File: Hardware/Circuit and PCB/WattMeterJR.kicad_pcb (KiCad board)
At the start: 4 copper layers, 66.6 x 82.1 mm, 51 parts, among them IC1 ATM90E32AS-AU-R, J1 502570-0893, J5 Input, J6 Debug, J7 PWR/GND, T1 CT1020, U2 ESP32-C6-WROOM-1-N8, Y1 16.384MHz

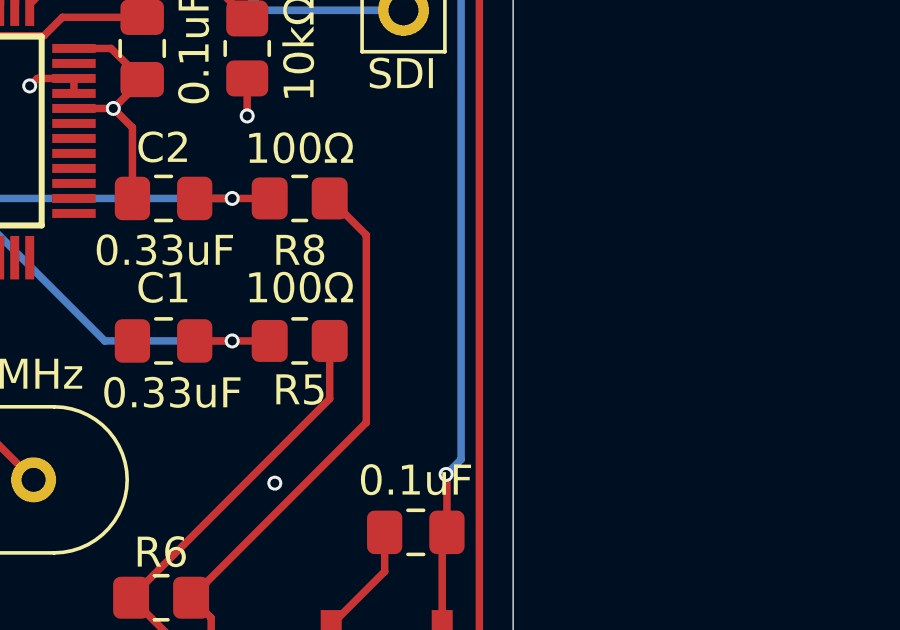
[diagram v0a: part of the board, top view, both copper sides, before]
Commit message: Add pullup for GPIO9
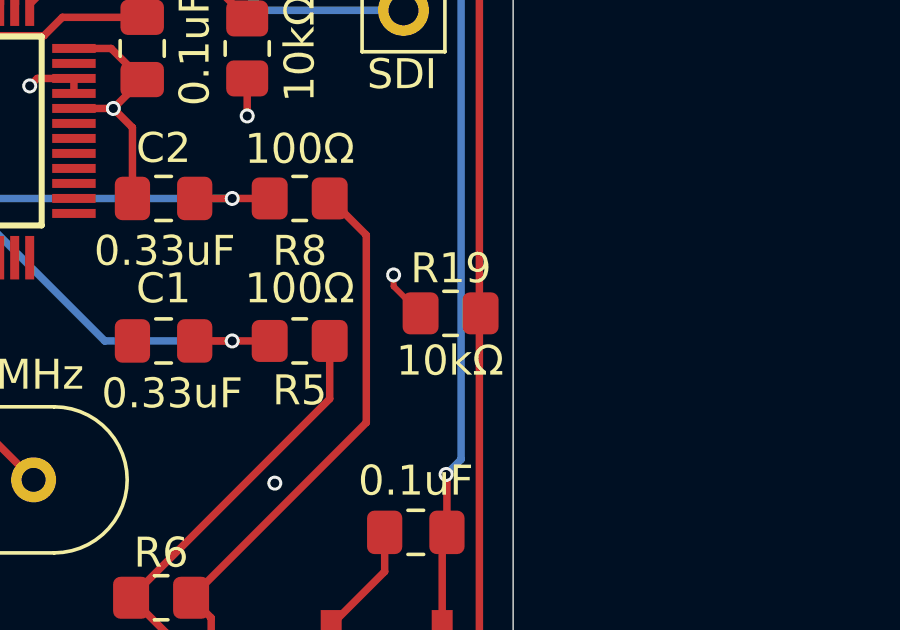
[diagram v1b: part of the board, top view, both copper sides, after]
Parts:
- added R19: 10kΩ, Resistor_SMD:R_0805_2012Metric_Pad1.20x1.40mm_HandSolder, F.Cu at (142.5, 134.1)
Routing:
- net VDD: track 38.5 -> 40.2 mm, vias 8 -> 9
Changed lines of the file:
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@@
 		)
 	)
+	(footprint "Resistor_SMD:R_0805_2012Metric_Pad1.20x1.40mm_HandSolder"
+		(layer "F.Cu")
+		(at 142.53 134.08 180)
+		(descr "Resistor SMD 0805 (2012 Metric), square (rectangular) end terminal, IPC-7351 nominal with elongated pad for handsoldering. (Body size source: IPC-SM-782 page 72, https://www.pcb-3d.com/wordpress/wp-content/uploads/ipc-sm-782a_amendment_1_and_2.pdf), generated with kicad-footprint-generator")
+		(tags "resistor handsolder")
+		(property "Reference" "R19"
+			(at -0.01 1.5 0)
+			(layer "F.SilkS")
+			(effects
+				(font
+					(size 1 1)
+					(thickness 0.15)
+				)
+			)
+		)
+		(property "Value" "10kΩ"
+			(at 0.02 -1.58 0)
+			(layer "F.SilkS")
+			(effects
+				(font
+					(size 1 1)
+					(thickness 0.15)
+				)
+			)
+		)
+		(property "Datasheet" "~"
+			(at 0 0 0)
+			(layer "F.Fab")
+			(hide yes)
+			(effects
+				(font
+					(size 1.27 1.27)
+					(thickness 0.15)
+				)
+			)
+		)
+		(property "Description" "Resistor, US symbol"
+			(at 0 0 0)
+			(layer "F.Fab")
+			(hide yes)
+			(effects
+				(font
+					(size 1.27 1.27)
+					(thickness 0.15)
+				)
+			)
+		)
+		(property ki_fp_filters "R_*")
+		(sheetname "/")
+		(sheetfile "WattMeterJR.kicad_sch")
+		(attr smd)
+		(fp_line
+			(start -0.227064 0.735)
+			(end 0.227064 0.735)
+			(stroke
+				(width 0.12)
+				(type solid)
+			)
+			(layer "F.SilkS")
+		)
+		(fp_line
+			(start -0.227064 -0.735)
+			(end 0.227064 -0.735)
+			(stroke
+				(width 0.12)
+				(type solid)
+			)
+			(layer "F.SilkS")
+		)
+		(fp_line
+			(start 1.85 0.95)
+			(end -1.85 0.95)
+			(stroke
+				(width 0.05)
+				(type solid)
+			)
+			(layer "F.CrtYd")
+		)
+		(fp_line
+			(start 1.85 -0.95)
+			(end 1.85 0.95)
+			(stroke
+				(width 0.05)
+				(type solid)
+			)
+			(layer "F.CrtYd")
+		)
+		(fp_line
+			(start -1.85 0.95)
+			(end -1.85 -0.95)
+			(stroke
+				(width 0.05)
+				(type solid)
+			)
+			(layer "F.CrtYd")
+		)
+		(fp_line
+			(start -1.85 -0.95)
+			(end 1.85 -0.95)
+			(stroke
+				(width 0.05)
+				(type solid)
+			)
+			(layer "F.CrtYd")
+		)
+		(fp_line
+			(start 1 0.625)
+			(end -1 0.625)
+			(stroke
+				(width 0.1)
+				(type solid)
+			)
+			(layer "F.Fab")
+		)
+		(fp_line
+			(start 1 -0.625)
+			(end 1 0.625)
+			(stroke
+				(width 0.1)
+				(type solid)
+			)
+			(layer "F.Fab")
+		)
+		(fp_line
+			(start -1 0.625)
+			(end -1 -0.625)
+			(stroke
+				(width 0.1)
+				(type solid)
+			)
+			(layer "F.Fab")
+		)
+		(fp_line
+			(start -1 -0.625)
+			(end 1 -0.625)
+			(stroke
+				(width 0.1)
+				(type solid)
+			)
+			(layer "F.Fab")
+		)
+		(fp_text user "${REFERENCE}"
+			(at 0 0 0)
+			(layer "F.Fab")
+			(effects
+				(font
+					(size 0.5 0.5)
+					(thickness 0.08)
+				)
+			)
+		)
+		(pad "1" smd roundrect
+			(at -1 0 180)
+			(size 1.2 1.4)
+			(layers "F.Cu" "F.Mask" "F.Paste")
+			(roundrect_rratio 0.208333)
+			(net 66 "DB_IO9")
+			(pintype "passive")
+		)
+		(pad "2" smd roundrect
+			(at 1 0 180)
+			(size 1.2 1.4)
+			(layers "F.Cu" "F.Mask" "F.Paste")
+			(roundrect_rratio 0.208333)
+			(net 2 "VDD")
+			(pintype "passive")
+		)
+		(embedded_fonts no)
+		(model "${KICAD9_3DMODEL_DIR}/Resistor_SMD.3dshapes/R_0805_2012Metric.step"
+			(offset
+				(xyz 0 0 0)
+			)
+			(scale
+				(xyz 1 1 1)
+			)
+			(rotate
+				(xyz 0 0 0)
+			)
+		)
+	)
 	(footprint "ATM90E32AS:QFP50P900X900X120-48N"
 		(layer "F.Cu")
@@
 	)
 	(segment
+		(start 140.63 132.8)
+		(end 140.63 133.18)
+		(width 0.2)
+		(layer "F.Cu")
+		(net 2)
+	)
+	(segment
 		(start 103.61 108.38)
 		(end 103.816826 108.38)
@@
 	)
 	(segment
+		(start 140.63 133.18)
+		(end 141.53 134.08)
+		(width 0.2)
+		(layer "F.Cu")
+		(net 2)
+	)
+	(segment
 		(start 119.25 125.75)
 		(end 119.75 125.25)
@@
 		(size 0.5)
 		(drill 0.3)
+		(layers "F.Cu" "B.Cu")
+		(net 2)
+	)
+	(via
+		(at 140.63 132.8)
+		(size 0.5)
+		(drill 0.3)
